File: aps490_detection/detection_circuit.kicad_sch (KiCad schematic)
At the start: 0 parts

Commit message: add some components
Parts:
- added BT1: Battery_Cell, symbol Device:Battery_Cell
- added D1, D2, D3: LED, symbol Device:LED
- added SW1: SW_SPST, symbol Switch:SW_SPST
- added SW2: SW_Push, symbol Switch:SW_Push
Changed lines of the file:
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@@
     (company "PFPU2")
   )
+  (symbol (lib_id "Device:LED") (at 138.43 88.9 0) (unit 1)
+    (in_bom yes) (on_board yes) (dnp no) (fields_autoplaced)
+    (property "Reference" "D2" (at 136.8425 82.55 0)
+      (effects (font (size 1.27 1.27)))
+    )
+    (property "Value" "LED" (at 136.8425 85.09 0)
+      (effects (font (size 1.27 1.27)))
+    )
+    (property "Footprint" "" (at 138.43 88.9 0)
+      (effects (font (size 1.27 1.27)) hide)
+    )
+    (property "Datasheet" "~" (at 138.43 88.9 0)
+      (effects (font (size 1.27 1.27)) hide)
+    )
+    (pin "1")
+    (pin "2")
+    (instances
+      (project "aps490_detection"
+        (path "/e118c919-9296-4265-a7f4-7c13f94290b1/bad03448-3ebc-42d0-be48-dd19294cc20c"
+          (reference "D2") (unit 1)
+        )
+      )
+    )
+  )
+  (symbol (lib_id "Device:LED") (at 138.43 99.06 0) (unit 1)
+    (in_bom yes) (on_board yes) (dnp no) (fields_autoplaced)
+    (property "Reference" "D3" (at 136.8425 92.71 0)
+      (effects (font (size 1.27 1.27)))
+    )
+    (property "Value" "LED" (at 136.8425 95.25 0)
+      (effects (font (size 1.27 1.27)))
+    )
+    (property "Footprint" "" (at 138.43 99.06 0)
+      (effects (font (size 1.27 1.27)) hide)
+    )
+    (property "Datasheet" "~" (at 138.43 99.06 0)
+      (effects (font (size 1.27 1.27)) hide)
+    )
+    (pin "1")
+    (pin "2")
+    (instances
+      (project "aps490_detection"
+        (path "/e118c919-9296-4265-a7f4-7c13f94290b1/bad03448-3ebc-42d0-be48-dd19294cc20c"
+          (reference "D3") (unit 1)
+        )
+      )
+    )
+  )
+  (symbol (lib_id "Switch:SW_Push") (at 176.53 78.74 0) (unit 1)
+    (in_bom yes) (on_board yes) (dnp no) (fields_autoplaced)
+    (property "Reference" "SW2" (at 176.53 71.12 0)
+      (effects (font (size 1.27 1.27)))
+    )
+    (property "Value" "SW_Push" (at 176.53 73.66 0)
+      (effects (font (size 1.27 1.27)))
+    )
+    (property "Footprint" "" (at 176.53 73.66 0)
+      (effects (font (size 1.27 1.27)) hide)
+    )
+    (property "Datasheet" "~" (at 176.53 73.66 0)
+      (effects (font (size 1.27 1.27)) hide)
+    )
+    (pin "1")
+    (pin "2")
+    (instances
+      (project "aps490_detection"
+        (path "/e118c919-9296-4265-a7f4-7c13f94290b1/bad03448-3ebc-42d0-be48-dd19294cc20c"
+          (reference "SW2") (unit 1)
+        )
+      )
+    )
+  )
+  (symbol (lib_id "Switch:SW_SPST") (at 175.26 102.87 0) (unit 1)
+    (in_bom yes) (on_board yes) (dnp no) (fields_autoplaced)
+    (property "Reference" "SW1" (at 175.26 96.52 0)
+      (effects (font (size 1.27 1.27)))
+    )
+    (property "Value" "SW_SPST" (at 175.26 99.06 0)
+      (effects (font (size 1.27 1.27)))
+    )
+    (property "Footprint" "" (at 175.26 102.87 0)
+      (effects (font (size 1.27 1.27)) hide)
+    )
+    (property "Datasheet" "~" (at 175.26 102.87 0)
+      (effects (font (size 1.27 1.27)) hide)
+    )
+    (pin "1")
+    (pin "2")
+    (instances
+      (project "aps490_detection"
+        (path "/e118c919-9296-4265-a7f4-7c13f94290b1/bad03448-3ebc-42d0-be48-dd19294cc20c"
+          (reference "SW1") (unit 1)
+        )
+      )
+    )
+  )
+  (symbol (lib_id "Device:LED") (at 138.43 80.01 0) (unit 1)
+    (in_bom yes) (on_board yes) (dnp no) (fields_autoplaced)
+    (property "Reference" "D1" (at 136.8425 73.66 0)
+      (effects (font (size 1.27 1.27)))
+    )
+    (property "Value" "LED" (at 136.8425 76.2 0)
+      (effects (font (size 1.27 1.27)))
+    )
+    (property "Footprint" "" (at 138.43 80.01 0)
+      (effects (font (size 1.27 1.27)) hide)
+    )
+    (property "Datasheet" "~" (at 138.43 80.01 0)
+      (effects (font (size 1.27 1.27)) hide)
+    )
+    (pin "1")
+    (pin "2")
+    (instances
+      (project "aps490_detection"
+        (path "/e118c919-9296-4265-a7f4-7c13f94290b1/bad03448-3ebc-42d0-be48-dd19294cc20c"
+          (reference "D1") (unit 1)
+        )
+      )
+    )
+  )
+  (symbol (lib_id "Device:Battery_Cell") (at 73.66 115.57 0) (unit 1)
+    (in_bom yes) (on_board yes) (dnp no) (fields_autoplaced)
+    (property "Reference" "BT1" (at 77.47 112.4585 0)
+      (effects (font (size 1.27 1.27)) (justify left))
+    )
+    (property "Value" "Battery_Cell" (at 77.47 114.9985 0)
+      (effects (font (size 1.27 1.27)) (justify left))
+    )
+    (property "Footprint" "" (at 73.66 114.046 90)
+      (effects (font (size 1.27 1.27)) hide)
+    )
+    (property "Datasheet" "~" (at 73.66 114.046 90)
+      (effects (font (size 1.27 1.27)) hide)
+    )
+    (pin "2")
+    (pin "1")
+    (instances
+      (project "aps490_detection"
+        (path "/e118c919-9296-4265-a7f4-7c13f94290b1/bad03448-3ebc-42d0-be48-dd19294cc20c"
+          (reference "BT1") (unit 1)
+        )
+      )
+    )
+  )
 )

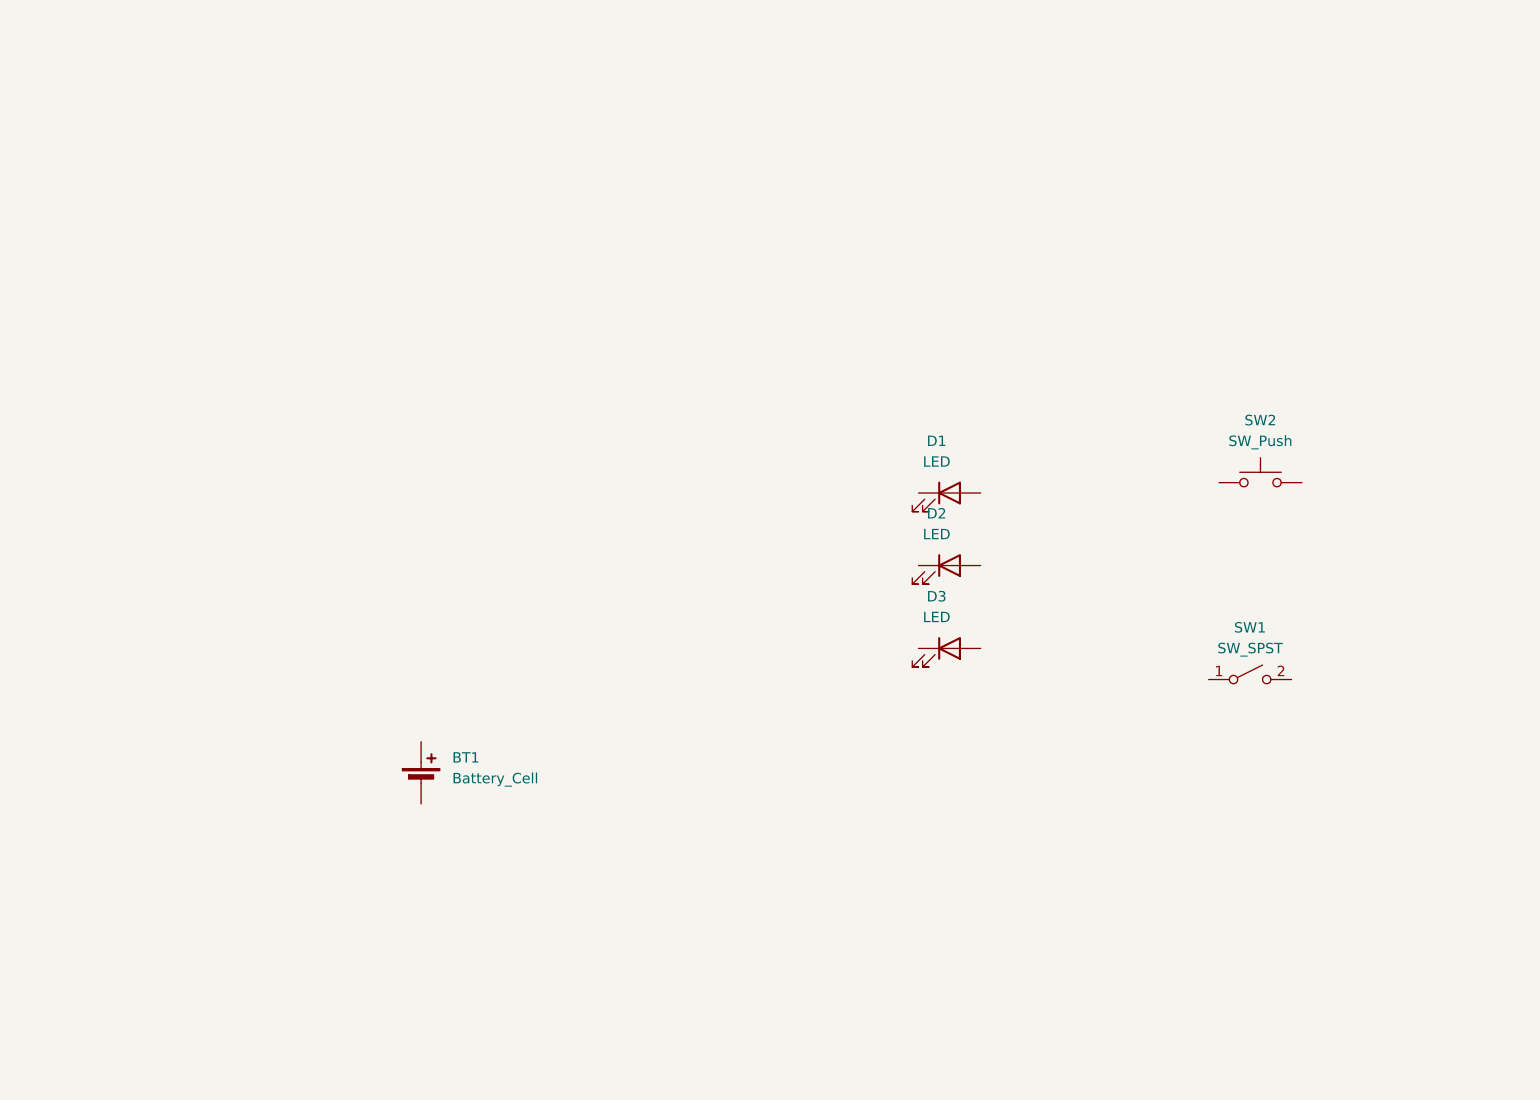
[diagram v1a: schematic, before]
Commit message: add lipo charger
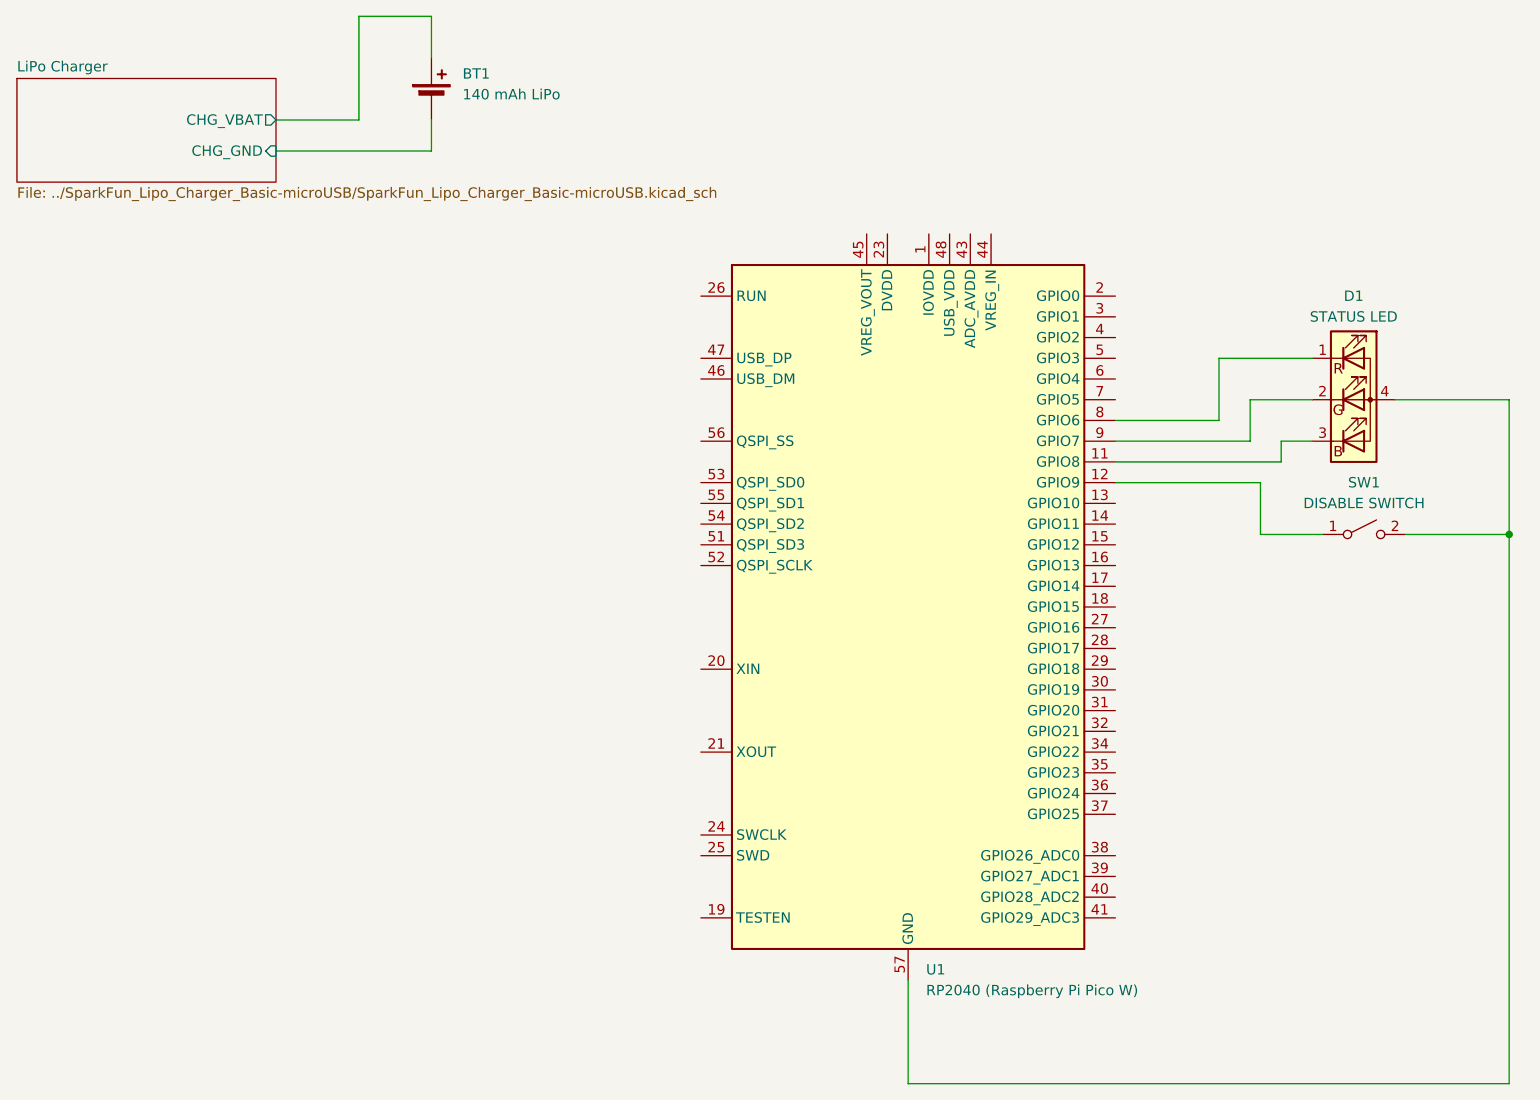
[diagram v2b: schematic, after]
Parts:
- removed D1, D2, D3: LED, symbol Device:LED
- removed SW2: SW_Push, symbol Switch:SW_Push
- added D1: STATUS LED, symbol Device:LED_RGBA
- added U1: RP2040 (Raspberry Pi Pico W), Package_DFN_QFN:QFN-56-1EP_7x7mm_P0.4mm_EP3.2x3.2mm, symbol MCU_RaspberryPi:RP2040
- BT1: value Battery_Cell -> 140 mAh LiPo
- SW1: value SW_SPST -> DISABLE SWITCH
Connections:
- net at SW1.1 (A): now also U1.12 (GPIO9)
- net at SW1.2 (B): now also D1.4 (A), U1.57 (GND)
- net LiPo Charger/CHG_VBAT: now reaches BT1.1 (+)
- net LiPo Charger/CHG_GND: now reaches BT1.2 (-)
- new net: D1.1 (RK), U1.8 (GPIO6)
- new net: D1.2 (GK), U1.9 (GPIO7)
- new net: D1.3 (BK), U1.11 (GPIO8)
- new net: U1.1 (IOVDD), U1.10 (IOVDD), U1.22 (IOVDD), U1.33 (IOVDD), U1.42 (IOVDD), U1.49 (IOVDD)
- new net: U1.23 (DVDD), U1.50 (DVDD)
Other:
- added sheet LiPo Charger (../SparkFun_Lipo_Charger_Basic-microUSB/SparkFun_Lipo_Charger_Basic-microUSB.kicad_sch)
- moved on the sheet: BT1, SW1

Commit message: update schematic
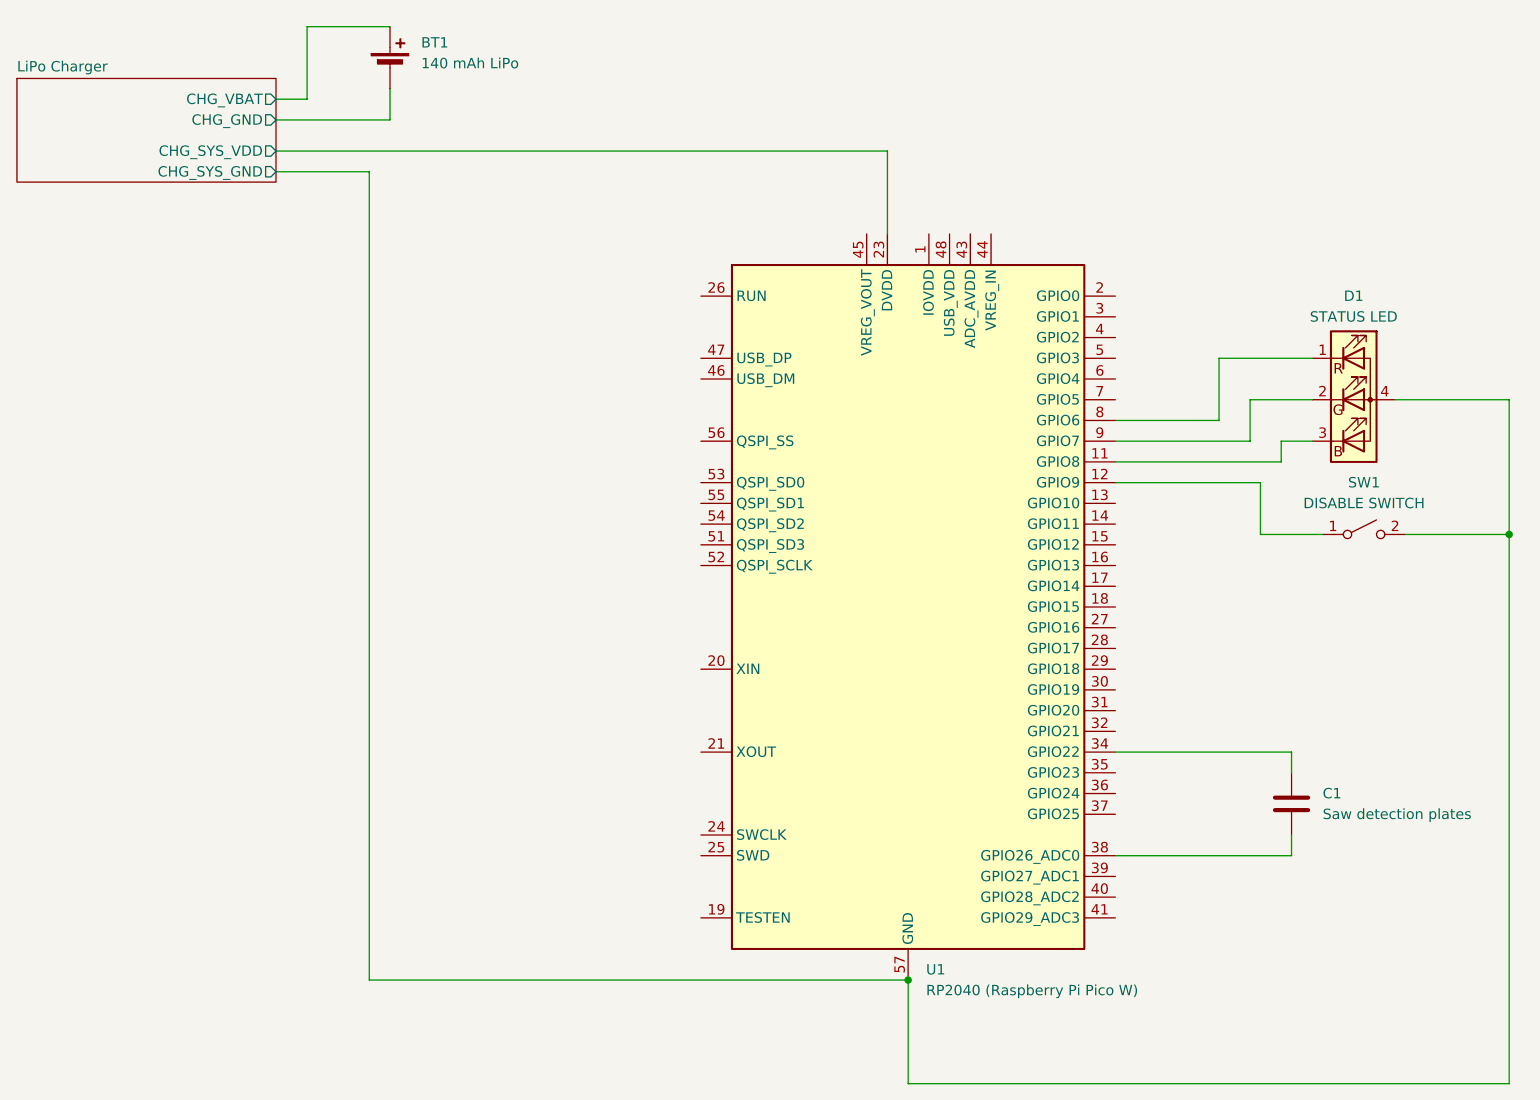
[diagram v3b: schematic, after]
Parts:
- added C1: Saw detection plates, symbol Device:C
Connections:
- net LiPo Charger/CHG_SYS_GND: now reaches D1.4 (A), SW1.2 (B), U1.57 (GND)
- net LiPo Charger/CHG_SYS_VDD: now reaches U1.23 (DVDD), U1.50 (DVDD)
- net at U1.34 (GPIO22): now also C1.1
- net at U1.38 (GPIO26_ADC0): now also C1.2
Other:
- sheet LiPo Charger ports: added CHG_SYS_GND, CHG_SYS_VDD; removed none
- title: Detection Circuit -> Autopsy Saw Detection Circuit
- moved on the sheet: BT1
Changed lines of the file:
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@@
   (paper "A4")
   (title_block
-    (title "Detection Circuit")
+    (title "Autopsy Saw Detection Circuit")
+    (date "2024-03-24")
+    (rev "3")
     (company "PFPU2")
   )
   (junction (at 207.01 85.09) (diameter 0) (color 0 0 0 0)
   )
-  (wire (pts (xy 66.04 21.59) (xy 74.93 21.59))
-    (stroke (width 0) (type default))
-  )
-  (wire (pts (xy 55.88 34.29) (xy 66.04 34.29))
-    (stroke (width 0) (type default))
+  (junction (at 133.35 139.7) (diameter 0) (color 0 0 0 0)
   )
   (wire (pts (xy 179.07 73.66) (xy 182.88 73.66))
@@
     (stroke (width 0) (type default))
   )
+  (wire (pts (xy 59.69 31.75) (xy 59.69 22.86))
+    (stroke (width 0) (type default))
+  )
+  (wire (pts (xy 55.88 38.1) (xy 130.81 38.1))
+    (stroke (width 0) (type default))
+  )
   (wire (pts (xy 171.45 71.12) (xy 171.45 63.5))
     (stroke (width 0) (type default))
   )
+  (wire (pts (xy 69.85 34.29) (xy 55.88 34.29))
+    (stroke (width 0) (type default))
+  )
+  (wire (pts (xy 180.34 121.92) (xy 180.34 124.46))
+    (stroke (width 0) (type default))
+  )
   (wire (pts (xy 194.31 85.09) (xy 207.01 85.09))
     (stroke (width 0) (type default))
   )
-  (wire (pts (xy 74.93 38.1) (xy 55.88 38.1))
-    (stroke (width 0) (type default))
-  )
   (wire (pts (xy 158.75 78.74) (xy 176.53 78.74))
     (stroke (width 0) (type default))
@@
     (stroke (width 0) (type default))
   )
-  (wire (pts (xy 74.93 34.29) (xy 74.93 38.1))
-    (stroke (width 0) (type default))
-  )
-  (wire (pts (xy 66.04 34.29) (xy 66.04 21.59))
+  (wire (pts (xy 180.34 124.46) (xy 158.75 124.46))
     (stroke (width 0) (type default))
   )
@@
     (stroke (width 0) (type default))
   )
+  (wire (pts (xy 55.88 31.75) (xy 59.69 31.75))
+    (stroke (width 0) (type default))
+  )
   (wire (pts (xy 158.75 71.12) (xy 171.45 71.12))
     (stroke (width 0) (type default))
@@
     (stroke (width 0) (type default))
   )
+  (wire (pts (xy 69.85 30.48) (xy 69.85 34.29))
+    (stroke (width 0) (type default))
+  )
   (wire (pts (xy 171.45 63.5) (xy 182.88 63.5))
     (stroke (width 0) (type default))
@@
     (stroke (width 0) (type default))
   )
-  (wire (pts (xy 74.93 21.59) (xy 74.93 26.67))
+  (wire (pts (xy 158.75 111.76) (xy 180.34 111.76))
+    (stroke (width 0) (type default))
+  )
+  (wire (pts (xy 180.34 111.76) (xy 180.34 114.3))
+    (stroke (width 0) (type default))
+  )
+  (wire (pts (xy 67.31 139.7) (xy 133.35 139.7))
+    (stroke (width 0) (type default))
+  )
+  (wire (pts (xy 55.88 40.64) (xy 67.31 40.64))
     (stroke (width 0) (type default))
   )
   (wire (pts (xy 175.26 73.66) (xy 175.26 68.58))
+    (stroke (width 0) (type default))
+  )
+  (wire (pts (xy 130.81 38.1) (xy 130.81 48.26))
+    (stroke (width 0) (type default))
+  )
+  (wire (pts (xy 67.31 40.64) (xy 67.31 139.7))
+    (stroke (width 0) (type default))
+  )
+  (wire (pts (xy 59.69 22.86) (xy 69.85 22.86))
     (stroke (width 0) (type default))
   )
@@
     )
   )
-  (symbol (lib_id "Device:Battery_Cell") (at 74.93 31.75 0) (unit 1)
-    (in_bom yes) (on_board yes) (dnp no) (fields_autoplaced)
-    (property "Reference" "BT1" (at 78.74 28.6385 0)
-      (effects (font (size 1.27 1.27)) (justify left))
-    )
-    (property "Value" "140 mAh LiPo" (at 78.74 31.1785 0)
-      (effects (font (size 1.27 1.27)) (justify left))
-    )
-    (property "Footprint" "" (at 74.93 30.226 90)
-      (effects (font (size 1.27 1.27)) hide)
-    )
-    (property "Datasheet" "~" (at 74.93 30.226 90)
+  (symbol (lib_id "Device:Battery_Cell") (at 69.85 27.94 0) (unit 1)
+    (in_bom yes) (on_board yes) (dnp no) (fields_autoplaced)
+    (property "Reference" "BT1" (at 73.66 24.8285 0)
+      (effects (font (size 1.27 1.27)) (justify left))
+    )
+    (property "Value" "140 mAh LiPo" (at 73.66 27.3685 0)
+      (effects (font (size 1.27 1.27)) (justify left))
+    )
+    (property "Footprint" "" (at 69.85 26.416 90)
+      (effects (font (size 1.27 1.27)) hide)
+    )
+    (property "Datasheet" "~" (at 69.85 26.416 90)
       (effects (font (size 1.27 1.27)) hide)
     )
@@
         (path "/e118c919-9296-4265-a7f4-7c13f94290b1/bad03448-3ebc-42d0-be48-dd19294cc20c"
           (reference "BT1") (unit 1)
+        )
+      )
+    )
+  )
+  (symbol (lib_id "Device:C") (at 180.34 118.11 0) (unit 1)
+    (in_bom yes) (on_board yes) (dnp no) (fields_autoplaced)
+    (property "Reference" "C1" (at 184.15 116.84 0)
+      (effects (font (size 1.27 1.27)) (justify left))
+    )
+    (property "Value" "Saw detection plates" (at 184.15 119.38 0)
+      (effects (font (size 1.27 1.27)) (justify left))
+    )
+    (property "Footprint" "" (at 181.3052 121.92 0)
+      (effects (font (size 1.27 1.27)) hide)
+    )
+    (property "Datasheet" "~" (at 180.34 118.11 0)
+      (effects (font (size 1.27 1.27)) hide)
+    )
+    (pin "2")
+    (pin "1")
+    (instances
+      (project "aps490_detection"
+        (path "/e118c919-9296-4265-a7f4-7c13f94290b1/bad03448-3ebc-42d0-be48-dd19294cc20c"
+          (reference "C1") (unit 1)
         )
       )
@@
     )
     (property "Sheetfile" "../SparkFun_Lipo_Charger_Basic-microUSB/SparkFun_Lipo_Charger_Basic-microUSB.kicad_sch" (at 24.13 42.4946 0)
-      (effects (font (size 1.27 1.27)) (justify left top))
-    )
-    (pin "CHG_VBAT" output (at 55.88 34.29 0)
+      (effects (font (size 1.27 1.27)) (justify left top) hide)
+    )
+    (pin "CHG_VBAT" output (at 55.88 31.75 0)
       (effects (font (size 1.27 1.27)) (justify right))
     )
-    (pin "CHG_GND" input (at 55.88 38.1 0)
+    (pin "CHG_GND" output (at 55.88 34.29 0)
       (effects (font (size 1.27 1.27)) (justify right))
     )
+    (pin "CHG_SYS_GND" output (at 55.88 40.64 0)
+      (effects (font (size 1.27 1.27)) (justify right))
+    )
+    (pin "CHG_SYS_VDD" output (at 55.88 38.1 0)
+      (effects (font (size 1.27 1.27)) (justify right))
+    )
